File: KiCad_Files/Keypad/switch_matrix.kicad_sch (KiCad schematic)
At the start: 43 parts

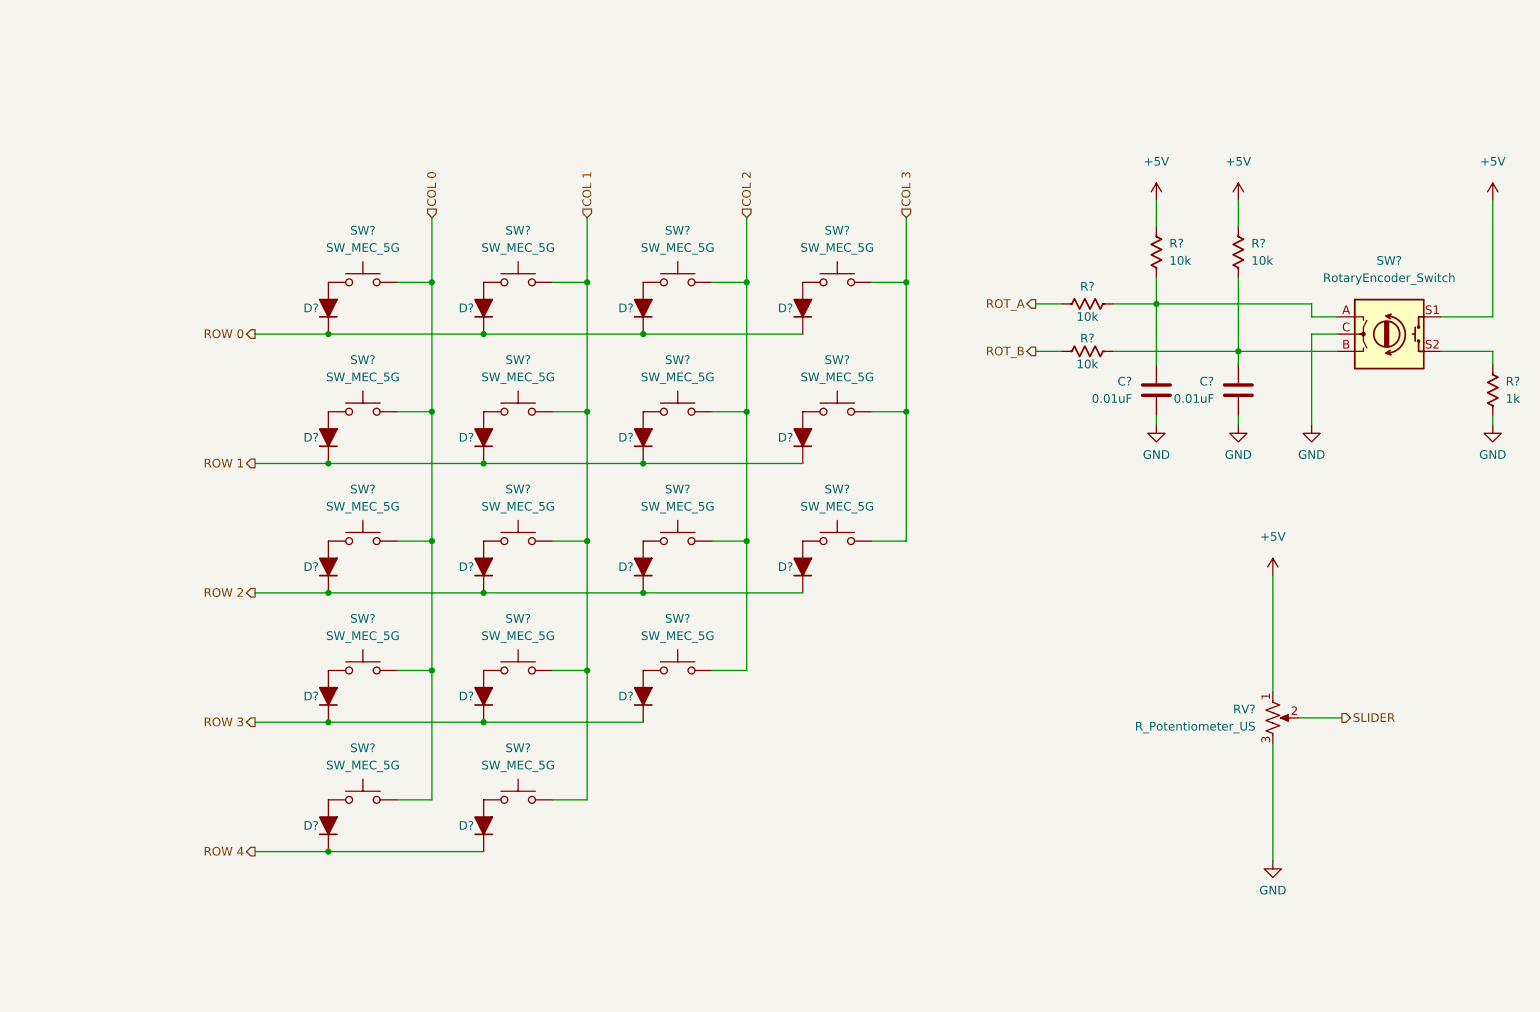
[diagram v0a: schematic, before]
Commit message: Added schematic for USB C, per key rgb led, 2 types of jtag connectors, rf connector, rotary encoder, slider, and OLED pins
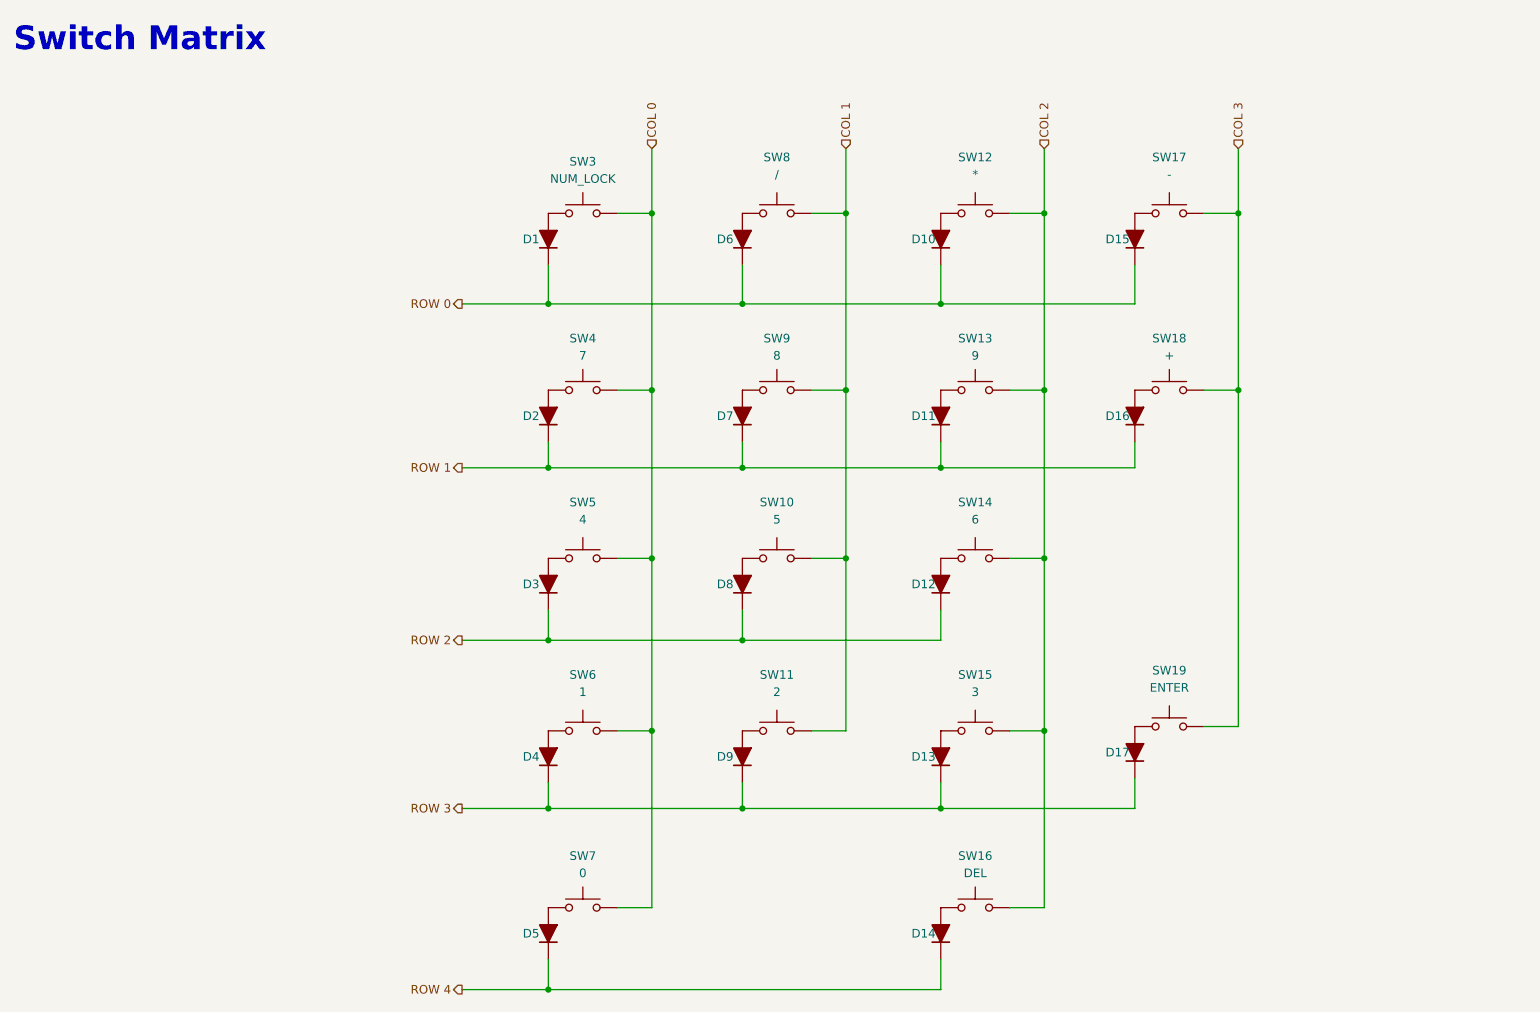
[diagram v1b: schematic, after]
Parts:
- removed C? (x2): 0.01uF, Capacitor_SMD_AKL:C_0603_1608Metric, symbol Capacitor_US_AKL:C_0603
- removed R? (x4): 10k, Resistor_SMD_AKL:R_0603_1608Metric, symbol Resistor_US_AKL:R_0603
- removed R?: 1k, Resistor_SMD_AKL:R_0603_1608Metric, symbol Resistor_US_AKL:R_0603
- removed RV?: R_Potentiometer_US, symbol Device:R_Potentiometer_US
- removed SW?: RotaryEncoder_Switch, symbol Device:RotaryEncoder_Switch
- SW10: renamed from SW?; value SW_MEC_5G -> 5
- SW11: renamed from SW?; value SW_MEC_5G -> 2
- SW12: renamed from SW?; value SW_MEC_5G -> *
- SW13: renamed from SW?; value SW_MEC_5G -> 9
- SW14: renamed from SW?; value SW_MEC_5G -> 6
- SW15: renamed from SW?; value SW_MEC_5G -> 3
- SW16: renamed from SW?; value SW_MEC_5G -> DEL
- SW17: renamed from SW?; value SW_MEC_5G -> -
- SW18: renamed from SW?; value SW_MEC_5G -> +
- SW19: renamed from SW?; value SW_MEC_5G -> ENTER
- SW3: renamed from SW?; value SW_MEC_5G -> NUM_LOCK
- SW4: renamed from SW?; value SW_MEC_5G -> 7
- SW5: renamed from SW?; value SW_MEC_5G -> 4
- SW6: renamed from SW?; value SW_MEC_5G -> 1
- SW7: renamed from SW?; value SW_MEC_5G -> 0
- SW8: renamed from SW?; value SW_MEC_5G -> /
- SW9: renamed from SW?; value SW_MEC_5G -> 8
- gave numbers to parts that had none: 17
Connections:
- net COL 1: no longer SW16.3 (B), SW16.4 (B)
- net COL 2: now also SW16.3 (B), SW16.4 (B)
- net ROW 2: no longer D17.1 (K)
- net ROW 3: now also D17.1 (K)
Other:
- note added: "Switch Matrix"
- moved on the sheet: D1, D10, D11, D12, D13, D14, D15, D16, D17, D2, D3, D4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
